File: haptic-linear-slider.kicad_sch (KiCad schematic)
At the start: 78 parts, among them IC1 DIO54335TST6, IC2 TLV61048DBVR, J1 SWD, J2 USB_C_Receptacle_USB2.0_16P, J3 TBC05-02-1-G-G, J4 EXT_CTRL, SW1 SW_Reset, SW2 SW_Boot, U1 RP2354A, U2 PSM01-081A-103B2, U3 DRV8876PWPR, U4 USBLC6-2SC6, Y1 ABM8-272-T3

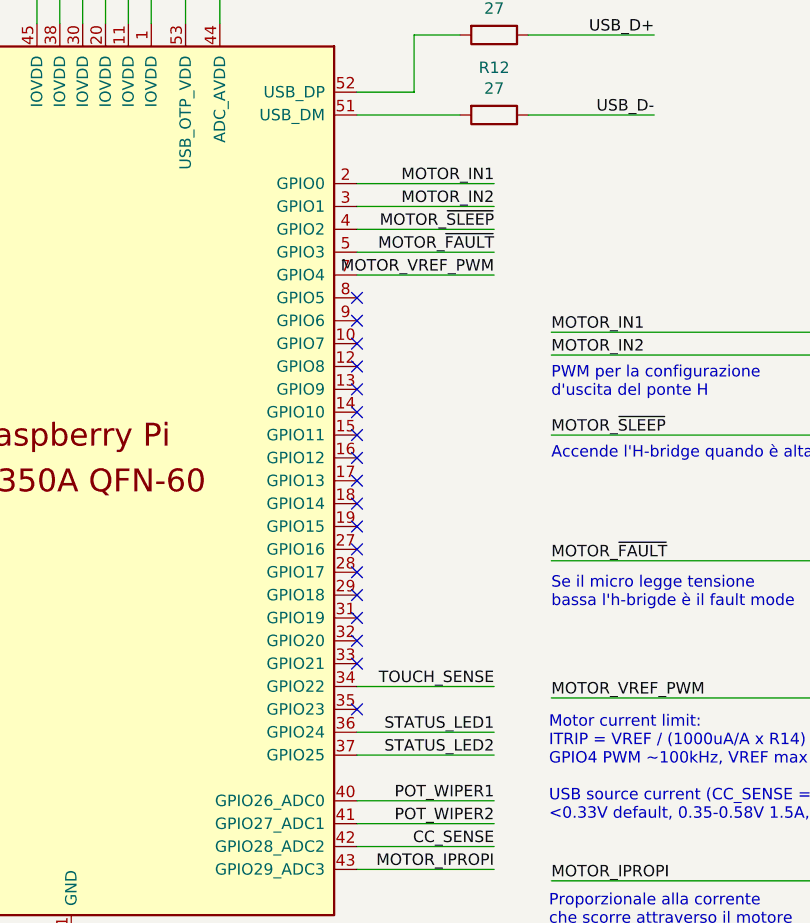
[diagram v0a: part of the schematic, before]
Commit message: Moved pin on micro for better routing
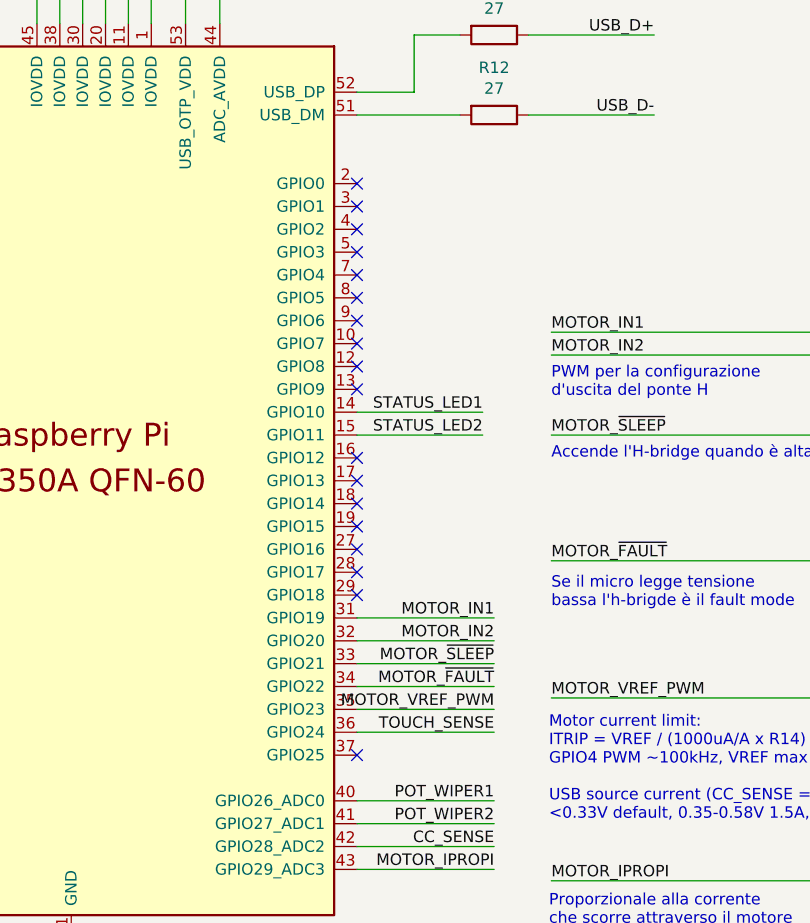
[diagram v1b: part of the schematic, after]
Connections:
- net MOTOR_IN1: now also U1.31 (GPIO19); no longer U1.2 (GPIO0)
- net MOTOR_IN2: now also U1.32 (GPIO20); no longer U1.3 (GPIO1)
- net MOTOR_VREF_PWM: now also U1.35 (GPIO23); no longer U1.7 (GPIO4)
- net MOTOR_~{FAULT}: now also U1.34 (GPIO22); no longer U1.5 (GPIO3)
- net MOTOR_~{SLEEP}: now also U1.33 (GPIO21); no longer U1.4 (GPIO2)
- net STATUS_LED1: now also U1.14 (GPIO10); no longer U1.36 (GPIO24)
- net STATUS_LED2: now also U1.15 (GPIO11); no longer U1.37 (GPIO25)
- net TOUCH_SENSE: now also U1.36 (GPIO24); no longer U1.34 (GPIO22)

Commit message: Condensatori
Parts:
- added C34: 10n, Capacitor_SMD:C_0805_2012Metric_Pad1.18x1.45mm_HandSolder, symbol Device:C
- added R26: 20k, Resistor_SMD:R_0805_2012Metric_Pad1.20x1.40mm_HandSolder, symbol Device:R
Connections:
- net GND: now also C34.2, R26.2; no longer U3.7 (IMODE)
- net MOTOR_IPROPI: now also C34.1
- new net: R26.1, U3.7 (IMODE)

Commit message: Ho fatto il layout di USB, convertitori DCDC e ponte H. Il layout della USB non so come si faccia e l'ho fatto a caso. Ho cambiato il piano superiore da GND a 3V3. Buonanotte Gengis.
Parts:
- removed R22: 10k, Resistor_SMD:R_0805_2012Metric_Pad1.20x1.40mm_HandSolder, symbol Device:R
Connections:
- net CC_SENSE: now also U1.43 (GPIO29_ADC3); no longer U1.42 (GPIO28_ADC2)
- net MOTOR_IN1: now also U1.35 (GPIO23); no longer U1.31 (GPIO19)
- net MOTOR_IN2: now also U1.34 (GPIO22); no longer U1.32 (GPIO20)
- net MOTOR_IPROPI: now also U1.40 (GPIO26_ADC0); no longer U1.43 (GPIO29_ADC3)
- net MOTOR_VREF_PWM: now also C33.1, R23.1, U1.31 (GPIO19), U3.5 (VREF); no longer U1.35 (GPIO23)
- net MOTOR_~{FAULT}: now also U1.32 (GPIO20); no longer U1.34 (GPIO22)
- net POT_WIPER1: now also U1.41 (GPIO27_ADC1); no longer U1.40 (GPIO26_ADC0)
- net POT_WIPER2: now also U1.42 (GPIO28_ADC2); no longer U1.41 (GPIO27_ADC1)
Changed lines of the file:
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@@
 	(wire
 		(pts
-			(xy 232.41 228.6) (xy 247.65 228.6)
-		)
-		(stroke
-			(width 0)
-			(type default)
-		)
-	)
-	(wire
-		(pts
 			(xy 144.78 153.67) (xy 144.78 146.05)
 		)
@@
 	(wire
 		(pts
-			(xy 232.41 223.52) (xy 247.65 223.52)
-		)
-		(stroke
-			(width 0)
-			(type default)
-		)
-	)
-	(wire
-		(pts
 			(xy 224.79 109.22) (xy 224.79 110.49)
 		)
@@
 	(wire
 		(pts
-			(xy 393.7 184.15) (xy 401.32 184.15)
+			(xy 232.41 223.52) (xy 247.65 223.52)
 		)
 		(stroke
@@
 	(wire
 		(pts
-			(xy 190.5 49.53) (xy 224.79 49.53)
+			(xy 393.7 184.15) (xy 401.32 184.15)
 		)
 		(stroke
@@
 	(wire
 		(pts
-			(xy 294.64 196.85) (xy 300.99 196.85)
+			(xy 190.5 49.53) (xy 224.79 49.53)
 		)
 		(stroke
@@
 	(wire
 		(pts
-			(xy 323.85 55.88) (xy 323.85 57.15)
+			(xy 294.64 196.85) (xy 300.99 196.85)
 		)
 		(stroke
@@
 	(wire
 		(pts
-			(xy 219.71 99.06) (xy 224.79 99.06)
+			(xy 323.85 55.88) (xy 323.85 57.15)
 		)
 		(stroke
@@
 	(wire
 		(pts
-			(xy 387.35 173.99) (xy 381 173.99)
+			(xy 219.71 99.06) (xy 224.79 99.06)
 		)
 		(stroke
@@
 	(wire
 		(pts
-			(xy 339.09 41.91) (xy 344.17 41.91)
+			(xy 387.35 173.99) (xy 381 173.99)
 		)
 		(stroke
@@
 	(wire
 		(pts
-			(xy 137.16 156.21) (xy 168.91 156.21)
+			(xy 339.09 41.91) (xy 344.17 41.91)
 		)
 		(stroke
@@
 	(wire
 		(pts
-			(xy 232.41 226.06) (xy 247.65 226.06)
+			(xy 137.16 156.21) (xy 168.91 156.21)
 		)
 		(stroke
@@
 	(wire
 		(pts
-			(xy 307.34 212.09) (xy 295.91 212.09)
-		)
-		(stroke
-			(width 0)
-			(type default)
-		)
-	)
-	(wire
-		(pts
 			(xy 232.41 210.82) (xy 247.65 210.82)
 		)
@@
 	(wire
 		(pts
-			(xy 288.29 212.09) (xy 254 212.09)
+			(xy 254 212.09) (xy 307.34 212.09)
 		)
 		(stroke
@@
 	(wire
 		(pts
+			(xy 232.41 228.6) (xy 247.65 228.6)
+		)
+		(stroke
+			(width 0)
+			(type default)
+		)
+	)
+	(wire
+		(pts
 			(xy 306.07 97.79) (xy 306.07 113.03)
 		)
@@
 	(wire
 		(pts
+			(xy 232.41 226.06) (xy 247.65 226.06)
+		)
+		(stroke
+			(width 0)
+			(type default)
+		)
+	)
+	(wire
+		(pts
 			(xy 44.45 96.52) (xy 44.45 86.36)
 		)
@@
 		)
 	)
-	(label "MOTOR_VREF_PWM"
+	(label "MOTOR_IN1"
 		(at 247.65 213.36 180)
 		(effects
@@
 		)
 	)
+	(label "POT_WIPER1"
+		(at 247.65 226.06 180)
+		(effects
+			(font
+				(size 1.27 1.27)
+			)
+			(justify right bottom)
+		)
+	)
 	(label "CC_SENSE"
 		(at 363.22 43.18 180)
@@
 		)
 	)
+	(label "POT_WIPER2"
+		(at 247.65 228.6 180)
+		(effects
+			(font
+				(size 1.27 1.27)
+			)
+			(justify right bottom)
+		)
+	)
 	(label "SWD"
 		(at 154.94 222.25 0)
@@
 		)
 	)
-	(label "MOTOR_IN1"
+	(label "MOTOR_VREF_PWM"
 		(at 247.65 203.2 180)
 		(effects
@@
 		)
 	)
-	(label "POT_WIPER1"
-		(at 247.65 223.52 180)
-		(effects
-			(font
-				(size 1.27 1.27)
-			)
-			(justify right bottom)
-		)
-	)
 	(label "MOTOR_~{FAULT}"
 		(at 254 196.85 0)
@@
 		)
 	)
-	(label "MOTOR_IN2"
+	(label "MOTOR_~{FAULT}"
 		(at 247.65 205.74 180)
 		(effects
@@
 		)
 	)
+	(label "CC_SENSE"
+		(at 247.65 231.14 180)
+		(effects
+			(font
+				(size 1.27 1.27)
+			)
+			(justify right bottom)
+		)
+	)
 	(label "XOUT"
 		(at 91.44 163.83 180)
@@
 		)
 	)
-	(label "MOTOR_~{FAULT}"
+	(label "MOTOR_IN2"
 		(at 247.65 210.82 180)
 		(effects
@@
 		)
 	)
-	(label "MOTOR_IPROPI"
-		(at 247.65 231.14 180)
-		(effects
-			(font
-				(size 1.27 1.27)
-			)
-			(justify right bottom)
-		)
-	)
 	(label "TOUCH_SENSE"
 		(at 58.42 240.03 180)
@@
 		)
 	)
-	(label "POT_WIPER2"
-		(at 247.65 226.06 180)
-		(effects
-			(font
-				(size 1.27 1.27)
-			)
-			(justify right bottom)
-		)
-	)
-	(label "CC_SENSE"
-		(at 247.65 228.6 180)
-		(effects
-			(font
-				(size 1.27 1.27)
-			)
-			(justify right bottom)
-		)
-	)
 	(label "USB_D-"
 		(at 332.74 50.8 180)
@@
 		)
 	)
+	(label "MOTOR_IPROPI"
+		(at 247.65 223.52 180)
+		(effects
+			(font
+				(size 1.27 1.27)
+			)
+			(justify right bottom)
+		)
+	)
 	(label "USB_D-"
 		(at 378.46 48.26 180)
@@
 					(unit 1)
 				)
-			)
-		)
-	)
-	(symbol
-		(lib_id "Device:R")
-		(at 292.1 212.09 90)
-		(unit 1)
-		(body_style 1)
-		(exclude_from_sim no)
-		(in_bom yes)
-		(on_board yes)
-		(in_pos_files yes)
-		(dnp no)
-		(property "Reference" "R22"
-			(at 290.6395 207.3275 90)
-			(show_name no)
-			(do_not_autoplace no)
-			(effects
-				(font
-					(size 1.27 1.27)
-				)
-				(justify right)
-			)
-		)
-		(property "Value" "10k"
-			(at 290.576 209.55 90)
-			(show_name no)
-			(do_not_autoplace no)
-			(effects
-				(font
-					(size 1.27 1.27)
-				)
-				(justify right)
-			)
-		)
-		(property "Footprint" "Resistor_SMD:R_0805_2012Metric_Pad1.20x1.40mm_HandSolder"
-			(at 292.1 213.868 90)
-			(hide yes)
-			(show_name no)
-			(do_not_autoplace no)
-			(effects
-				(font
-					(size 1.27 1.27)
-				)
-			)
-		)
-		(property "Datasheet" "~"
-			(at 292.1 212.09 0)
-			(hide yes)
-			(show_name no)
-			(do_not_autoplace no)
-			(effects
-				(font
-					(size 1.27 1.27)
-				)
-			)
-		)
-		(property "Description" ""
-			(at 292.1 212.09 0)
-			(show_name no)
-			(do_not_autoplace no)
-			(effects
-				(font
-					(size 1.27 1.27)
-				)
-			)
-		)
-		(property "Manufacturer_Name" "YAGEO"
-			(at 292.1 212.09 0)
-			(hide yes)
-			(show_name no)
-			(do_not_autoplace no)
-			(effects
-				(font
-					(size 1.27 1.27)
-				)
-			)
-		)
-		(property "Manufacturer_Part_Number" "RC0805FR-0710KL"
-			(at 292.1 212.09 0)
-			(hide yes)
-			(show_name no)
-			(do_not_autoplace no)
-			(effects
-				(font
-					(size 1.27 1.27)
-				)
-			)
-		)
-		(property "Mouser Part Number" "603-RC0805FR-0710KL"
-			(at 292.1 212.09 0)
-			(hide yes)
-			(show_name no)
-			(do_not_autoplace no)
-			(effects
-				(font
-					(size 1.27 1.27)
-				)
-			)
-		)
-		(property "Mouser Price/Stock" "https://www.mouser.it/ProductDetail/603-RC0805FR-0710KL"
-			(at 292.1 212.09 0)
-			(hide yes)
-			(show_name no)
-			(do_not_autoplace no)
-			(effects
-				(font
-					(size 1.27 1.27)
-				)
-			)
-		)
-		(pin "1"
-		)
-		(pin "2"
-		)
-		(instances
-			(project "haptic-linear-slider"
-				(path "/f60d71f9-9a8e-4a62-960d-f7b9664aea76"
-					(reference "R22")
-					(unit 1)
-				)

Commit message: nuovo micro e altro IC che si saldano meglio, routing rifatto ma va ancora rivisto
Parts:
- removed C12: 4u7, _Footprints:C_0402_1005Metric_small_pads, symbol Device:C
- removed C15, C16, C20, C22, C23, C24, C25, C26: 100n, _Footprints:C_0402_1005Metric_small_pads, symbol Device:C
- removed C4, C5: 15p, Capacitor_SMD:C_0603_1608Metric_Pad1.08x0.95mm_HandSolder, symbol Device:C
- removed L3: 3u3, _Footprints:L_pol_2016, symbol Device:L
- removed R11, R12: 27, Resistor_SMD:R_0805_2012Metric_Pad1.20x1.40mm_HandSolder, symbol Device:R
- removed R6: 1k, Resistor_SMD:R_0805_2012Metric_Pad1.20x1.40mm_HandSolder, symbol Device:R
- removed R9: 33, Resistor_SMD:R_0805_2012Metric_Pad1.20x1.40mm_HandSolder, symbol Device:R
- removed Y1: ABM8-272-T3, _Footprints:ABM8-272-T3, symbol Device:Crystal_GND24
- added H1, H2, H3: MountingHole, MountingHole:MountingHole_3.2mm_M3, symbol Mechanical:MountingHole
- added R7: 100k, Resistor_SMD:R_0805_2012Metric_Pad1.20x1.40mm_HandSolder, symbol Device:R
- added U7: TPS22918DBVR, Package_TO_SOT_SMD:SOT-23-6, symbol _Symbols:5.5V 2A Load Switch (Texas Instruments)
- C11, C13: value 4u7 -> 1u; footprint _Footprints:C_0402_1005Metric_small_pads -> Capacitor_SMD:C_0805_2012Metric_Pad1.18x1.45mm_HandSolder; Manufacturer_Part_Number CL05A475MO5NUNC -> CL21B105KBFNNNG; Mouser Part Number 187-CL05A475MO5NUNC -> 187-CL21B105KBFNNNG; Mouser Price/Stock https://www.mouser.it/en/ProductDetail/Samsung-Electro-Mechanics/CL05A475MO5NUNC?qs=5aG0NVq1C4xnuxNjQNWCEw%3D%3D -> https://www.mouser.it/en/ProductDetail/Samsung-Electro-Mechanics/CL21B105KBFNNNG?qs=hqM3L16%252Bxlf%252BLSavaAk0sA%3D%3D
- C17: value 100n -> 3n3; footprint _Footprints:C_0402_1005Metric_small_pads -> Capacitor_SMD:C_0805_2012Metric_Pad1.18x1.45mm_HandSolder; Manufacturer_Part_Number CL05B104KO5NFNC -> CL21B332KBANNNC; Mouser Part Number 187-CL05B104KO5NFNC -> 187-CL21B332KBANNNC; Mouser Price/Stock https://www.mouser.it/en/ProductDetail/Samsung-Electro-Mech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 -> https://www.mouser.com/ProductDetail/Samsung-Electro-Mechan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
- C21: value 100n -> 47u; footprint _Footprints:C_0402_1005Metric_small_pads -> Capacitor_SMD:C_1210_3225Metric_Pad1.33x2.70mm_HandSolder; Manufacturer_Name Samsung Electro-Mechanics -> Murata; Manufacturer_Part_Number CL05B104KO5NFNC -> GRM32ER61A476KE20L; Mouser Part Number 187-CL05B104KO5NFNC -> (none); Mouser Price/Stock https://www.mouser.it/en/ProductDetail/Samsung-Electro-Mech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 -> (none)
- C22: renamed from C18; footprint _Footprints:C_0402_1005Metric_small_pads -> Capacitor_SMD:C_0805_2012Metric_Pad1.18x1.45mm_HandSolder; Manufacturer_Part_Number CL05B104KO5NFNC -> CL21B104KBFNNNG; Mouser Part Number 187-CL05B104KO5NFNC -> 187-CL21B104KBFNNNG; Mouser Price/Stock https://www.mouser.it/en/ProductDetail/Samsung-Electro-Mech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 -> https://www.mouser.it/ProductDetail/187-CL21B104KBFNNNG
- C23: renamed from C19; value 100n -> 4u7; footprint _Footprints:C_0402_1005Metric_small_pads -> Capacitor_SMD:C_0805_2012Metric_Pad1.18x1.45mm_HandSolder; Manufacturer_Part_Number CL05B104KO5NFNC -> CL21A475KAQNNNE; Mouser Part Number 187-CL05B104KO5NFNC -> 187-CL21A475KAQNNNE; Mouser Price/Stock https://www.mouser.it/en/ProductDetail/Samsung-Electro-Mech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 -> https://www.mouser.com/ProductDetail/Samsung-Electro-Mechan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
- D2, D3: footprint LED_SMD:LED_0603_1608Metric -> LED_SMD:LED_0805_2012Metric_Pad1.15x1.40mm_HandSolder; Manufacturer_Part_Number 150060VS75000 -> 150080VS75000; Mouser Part Number 710-150060VS75000 -> 710-150080VS75000; Mouser Price/Stock https://www.mouser.it/ProductDetail/710-150060VS75000 -> https://www.mouser.it/ProductDetail/710-150080VS75000
- D4: footprint LED_SMD:LED_0603_1608Metric -> LED_SMD:LED_0805_2012Metric_Pad1.15x1.40mm_HandSolder; Manufacturer_Part_Number 150060RS75000 -> 150080RS75000; Mouser Part Number 710-150060RS75000 -> 710-150080RS75000; Mouser Price/Stock https://www.mouser.it/ProductDetail/710-150060RS75000 -> https://www.mouser.it/ProductDetail/710-150080RS75000
- U1: value RP2354A -> STM32C071KBT6; footprint _Footprints:RP2354A_QFN-60-1EP_7x7mm_P0.4mm_EP3.4x3.4mm -> Package_QFP:LQFP-32_7x7mm_P0.8mm; symbol MCU_RaspberryPi_RP2350:RP2350_60QFN -> MCU_ST_STM32C0:STM32C071KBTx; Manufacturer_Name Raspberry Pi -> STMicroelectronics; Manufacturer_Part_Number SC1511(13)-A4 -> STM32C071KBT6; Mouser Part Number 358-SC151113 -> 511-STM32C071KBT6; Mouser Price/Stock https://www.mouser.it/en/ProductDetail/Raspberry-Pi/SC15111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 -> https://www.mouser.com/ProductDetail/STMicroelectronics/STM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
- renumbered C2 to C1, C9 to C10, C14 to C15, C3 to C2, C1 to C3, C27 to C31, C28 to C32, C29 to C35, C30 to C36, C31 to C37, C32 to C38, C10 to C9, J4 to J1, J1 to J2, J2 to J3, J3 to J4, R10 to R11, R13 to R14, R23 to R15, R14 to R16, R26 to R17, R17 to R18, R18 to R19, R15 to R20, R16 to R21, R24 to R22, R25 to R23, R19 to R24, R20 to R25, R21 to R26, R3 to R4, R4 to R5, R7 to R6, R5 to R9, U4 to U3, U3 to U4, IC1 to U5, IC2 to U6
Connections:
- net XOUT is gone; now on net USB_D-: U1.22 (PA11)
- net +3V3: now also SW2.1, U1.4 (VDD); no longer C11.1, C21.1, U1.1 (IOVDD), U1.11 (IOVDD), U1.20 (IOVDD), U1.30 (IOVDD), U1.38 (IOVDD), U1.44 (ADC_AVDD), U1.45 (IOVDD), U1.49 (VREG_VIN), U1.53 (USB_OTP_VDD), U1.54 (QSPI_IOVDD)
- net +5V: now also C11.1, R7.1, U7.1 (VIN); no longer C9.1, L2.2, U6.4 (EN), U6.5 (VIN)
- net CC_SENSE: now also U1.18 (PA8); no longer U1.43 (GPIO29_ADC3)
- net GND: now also U1.5 (VSS), U7.2 (GND); no longer SW2.1, U1.47 (VREG_PGND), U1.61 (GND)
- net MOTOR_IN1: now also U1.8 (PA1); no longer U1.35 (GPIO23)
- net MOTOR_IN2: now also U1.7 (PA0); no longer U1.34 (GPIO22)
- net MOTOR_IPROPI: now also U1.12 (PA5); no longer U1.40 (GPIO26_ADC0)
- net MOTOR_VREF_PWM: now also U1.11 (PA4); no longer U1.31 (GPIO19)
- net MOTOR_~{FAULT}: now also U1.10 (PA3); no longer U1.32 (GPIO20)
- net MOTOR_~{SLEEP}: now also U1.9 (PA2); no longer U1.33 (GPIO21)
- net POT_WIPER1: now also U1.13 (PA6); no longer U1.41 (GPIO27_ADC1)
- net POT_WIPER2: now also U1.14 (PA7); no longer U1.42 (GPIO28_ADC2)
- net STATUS_LED1: now also U1.27 (PB3); no longer U1.14 (GPIO10)
- net STATUS_LED2: now also U1.28 (PB4); no longer U1.15 (GPIO11)
- net SWCLK: now also J2.3 (Pin_3), R11.1, U1.25 (PA14); no longer J2.2 (Pin_2), U1.24 (SWCLK)
- net SWD: now also J2.2 (Pin_2), U1.24 (PA13); no longer J2.3 (Pin_3), U1.25 (SWD)
- net TOUCH_SENSE: now also U1.31 (PB7); no longer U1.36 (GPIO24)
- net USB_D+: now also U1.23 (PA12); no longer J3.A6 (D+), J3.B6 (D+), U3.6 (I/O1)
- net USB_D-: no longer J3.A7 (D-), J3.B7 (D-), U3.4 (I/O2)
- net LS_ON: now reaches C13.1
- net LS_ON: now also R7.2, U7.3 (ON); no longer U1.46 (VREG_AVDD)
- net MOTOR_OUT2: now reaches J4.1, U4.10 (OUT2)
- net MOTOR_OUT1: now reaches J4.2, U4.8 (OUT1)
- net BOOST_SW: now reaches D1.2 (A), L2.1, U6.1 (SW)
- net BUCK_SW: now reaches C6.1, L1.1, U5.2 (SW)
- removed net +1V1: C17.1, U1.23 (DVDD), U1.39 (DVDD), U1.50 (VREG_FB), U1.6 (DVDD)
- net CC1: no longer names the net of J3.A5 (CC1), R21.1, R22.1
- net CC2: no longer names the net of J3.B5 (CC2), R20.1, R23.1
- net RUN renamed NRST
- net NRST: now also U1.6 (PF2); no longer U1.26 (RUN)
- net XIN: no longer names the net of U1.21 (PA10)
- net ~{USB_BOOT} renamed BOOT0
- new net: J3.A6 (D+), J3.B6 (D+), U3.6 (I/O1)
- new net: J3.A7 (D-), J3.B7 (D-), U3.4 (I/O2)
- new net +5V_MOT: C21.1, C9.1, L2.2, U6.4 (EN), U6.5 (VIN), U7.6 (VOUT)
- new net LS_CT: C17.1, U7.4 (CT)
- no-connect marks 26 -> 17
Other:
- note added: "10V Power + In-rush Limiter"
- note added: "BOOT0 = PA14 (shared with SWCLK). Hold BOOT, tap RESET -> USB DFU bootloader. A blank chip starts in DFU on its own. If BOOT is ignored later, clear nBOOT_SEL once (CubeProgrammer)."
- note added: "Microcontroller"
- note added: "Motor current limit: ITRIP = VREF / (1000uA/A x R16) PA4 (TIM14) PWM ~100kHz, VREF max 3.0V -> 1.1A USB source current (CC_SENSE = Vcc/2): <0.33V default, 0.35-0.58V 1.5A, 0.66-1.02V 3A"
- note removed: "10V Power"
- note removed: "12MHz Crystal"
- note removed: "1V1 Power"
- note removed: "Motor current limit: ITRIP = VREF / (1000uA/A x R14) GPIO4 PWM ~100kHz, VREF max 3.0V -> 1.1A USB source current (CC_SENSE = Vcc/2): <0.33V default, 0.35-0.58V 1.5A, 0.66-1.02V 3A"
- moved on the sheet: C10, C15, C22, C23, C3, C6, C7, C8, J1, J2, L1, R11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
